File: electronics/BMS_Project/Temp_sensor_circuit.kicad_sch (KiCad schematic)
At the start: 0 parts

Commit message: added thermistor voltage divider to "temp_sensor_circuit"
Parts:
- added R29, R30, R31, R32: 100k, symbol Device:R
- added Temp_1, Temp_2, Temp_3, Temp_4: Prototyping_Pad_Data, BMS_lib:Prototyping_Pad_Data, symbol BMS_lib:Prototyping_Pad_Data
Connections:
- new net +5V: R29.2, R30.2, R31.2, R32.2
- new net Temp_1: R29.1, Temp_1.1
- new net Temp_2: R30.1, Temp_2.1
- new net Temp_3: R31.1, Temp_3.1
- new net Temp_4: R32.1, Temp_4.1

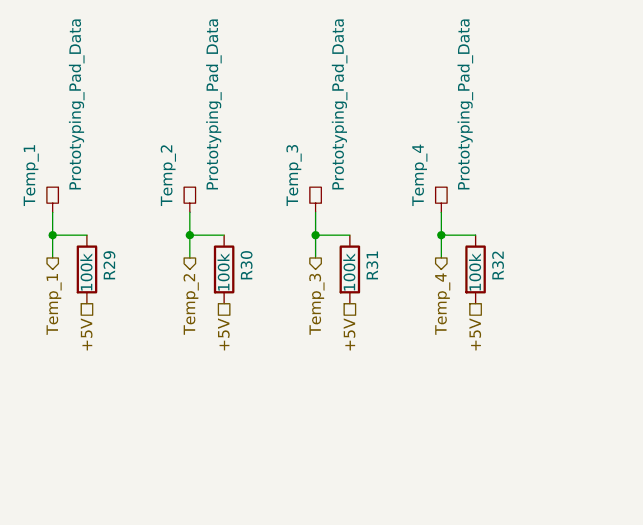
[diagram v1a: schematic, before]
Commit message: small tweaks to the labels
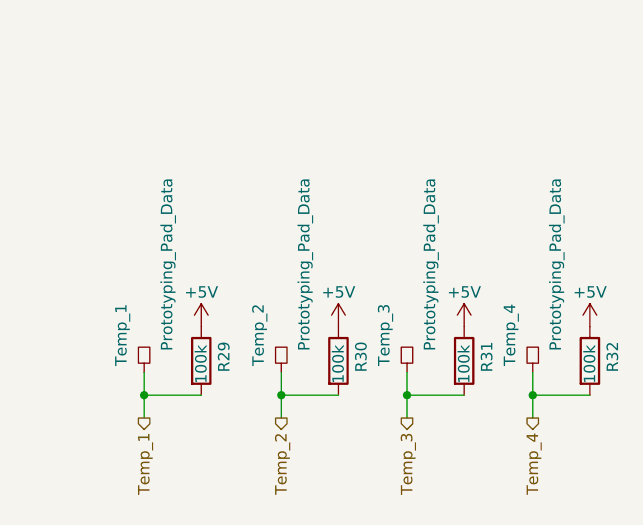
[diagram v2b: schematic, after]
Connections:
- net +5V: now also R29.1, R30.1, R31.1, R32.1; no longer R29.2, R30.2, R31.2, R32.2
- net Temp_1: now also R29.2; no longer R29.1
- net Temp_2: now also R30.2; no longer R30.1
- net Temp_3: now also R31.2; no longer R31.1
- net Temp_4: now also R32.2; no longer R32.1
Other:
- moved on the sheet: R29, R30, R31, R32, Temp_1, Temp_2, Temp_3, Temp_4

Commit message: Meeting 28.04.2023 worked on schematic
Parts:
- removed Temp_1, Temp_2, Temp_3, Temp_4: Prototyping_Pad_Data, BMS_lib:Prototyping_Pad_Data, symbol BMS_lib:Prototyping_Pad_Data
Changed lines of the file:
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@@
     (effects (font (size 1.27 1.27)) (justify right))
+  )
+  (hierarchical_label "sensor_3" (shape input) (at 80.01 50.8 90) (fields_autoplaced)
+    (effects (font (size 1.27 1.27)) (justify left))
+  )
+  (hierarchical_label "sensor_1" (shape input) (at 50.8 50.8 90) (fields_autoplaced)
+    (effects (font (size 1.27 1.27)) (justify left))
   )
   (hierarchical_label "Temp_3" (shape output) (at 80.01 55.88 270) (fields_autoplaced)
     (effects (font (size 1.27 1.27)) (justify right))
   )
+  (hierarchical_label "sensor_2" (shape input) (at 66.04 50.8 90) (fields_autoplaced)
+    (effects (font (size 1.27 1.27)) (justify left))
+  )
   (hierarchical_label "Temp_1" (shape output) (at 50.8 55.88 270) (fields_autoplaced)
     (effects (font (size 1.27 1.27)) (justify right))
   )
+  (hierarchical_label "sensor_4" (shape input) (at 93.98 50.8 90) (fields_autoplaced)
+    (effects (font (size 1.27 1.27)) (justify left))
+  )
   (hierarchical_label "Temp_2" (shape output) (at 66.04 55.88 270) (fields_autoplaced)
     (effects (font (size 1.27 1.27)) (justify right))
@@
     )
   )
-  (symbol (lib_id "BMS_lib:Prototyping_Pad_Data") (at 80.01 50.8 90) (unit 1)
-    (in_bom yes) (on_board yes) (dnp no)
-    (property "Reference" "Temp_3" (at 77.47 43.18 0)
-      (effects (font (size 1.27 1.27)) (justify right))
-    )
-    (property "Value" "Prototyping_Pad_Data" (at 82.55 29.21 0)
-      (effects (font (size 1.27 1.27)) (justify right))
-    )
-    (property "Footprint" "BMS_lib:Prototyping_Pad_Data" (at 76.2 46.99 0)
-      (effects (font (size 1.27 1.27)) hide)
-    )
-    (property "Datasheet" "" (at 80.01 50.8 0)
-      (effects (font (size 1.27 1.27)) hide)
-    )
-    (pin "1")
-    (instances
-      (project "BMS_Project"
-        (path "/524e7f14-feb0-4ca2-9425-a347c869bfa6/3ef60c79-05b1-4258-868e-74de6ac64829"
-          (reference "Temp_3") (unit 1)
-        )
-      )
-    )
-  )
-  (symbol (lib_id "BMS_lib:Prototyping_Pad_Data") (at 66.04 50.8 90) (unit 1)
-    (in_bom yes) (on_board yes) (dnp no)
-    (property "Reference" "Temp_2" (at 63.5 43.18 0)
-      (effects (font (size 1.27 1.27)) (justify right))
-    )
-    (property "Value" "Prototyping_Pad_Data" (at 68.58 29.21 0)
-      (effects (font (size 1.27 1.27)) (justify right))
-    )
-    (property "Footprint" "BMS_lib:Prototyping_Pad_Data" (at 62.23 46.99 0)
-      (effects (font (size 1.27 1.27)) hide)
-    )
-    (property "Datasheet" "" (at 66.04 50.8 0)
-      (effects (font (size 1.27 1.27)) hide)
-    )
-    (pin "1")
-    (instances
-      (project "BMS_Project"
-        (path "/524e7f14-feb0-4ca2-9425-a347c869bfa6/3ef60c79-05b1-4258-868e-74de6ac64829"
-          (reference "Temp_2") (unit 1)
-        )
-      )
-    )
-  )
-  (symbol (lib_id "BMS_lib:Prototyping_Pad_Data") (at 93.98 50.8 90) (unit 1)
-    (in_bom yes) (on_board yes) (dnp no)
-    (property "Reference" "Temp_4" (at 91.44 43.18 0)
-      (effects (font (size 1.27 1.27)) (justify right))
-    )
-    (property "Value" "Prototyping_Pad_Data" (at 96.52 29.21 0)
-      (effects (font (size 1.27 1.27)) (justify right))
-    )
-    (property "Footprint" "BMS_lib:Prototyping_Pad_Data" (at 90.17 46.99 0)
-      (effects (font (size 1.27 1.27)) hide)
-    )
-    (property "Datasheet" "" (at 93.98 50.8 0)
-      (effects (font (size 1.27 1.27)) hide)
-    )
-    (pin "1")
-    (instances
-      (project "BMS_Project"
-        (path "/524e7f14-feb0-4ca2-9425-a347c869bfa6/3ef60c79-05b1-4258-868e-74de6ac64829"
-          (reference "Temp_4") (unit 1)
-        )
-      )
-    )
-  )
   (symbol (lib_id "Device:R") (at 100.33 49.53 0) (unit 1)
     (in_bom yes) (on_board yes) (dnp no)
@@
         )
       )
-    )
-  )
-  (symbol (lib_id "BMS_lib:Prototyping_Pad_Data") (at 50.8 50.8 90) (unit 1)
-    (in_bom yes) (on_board yes) (dnp no)
-    (property "Reference" "Temp_1" (at 48.26 43.18 0)
-      (effects (font (size 1.27 1.27)) (justify right))
-    )
-    (property "Value" "Prototyping_Pad_Data" (at 53.34 29.21 0)
-      (effects (font (size 1.27 1.27)) (justify right))
-    )
-    (property "Footprint" "BMS_lib:Prototyping_Pad_Data" (at 46.99 46.99 0)
-      (effects (font (size 1.27 1.27)) hide)
-    )
-    (property "Datasheet" "" (at 50.8 50.8 0)
-      (effects (font (size 1.27 1.27)) hide)
-    )
-    (pin "1")
-    (instances
-      (project "BMS_Project"
-        (path "/524e7f14-feb0-4ca2-9425-a347c869bfa6/3ef60c79-05b1-4258-868e-74de6ac64829"
-          (reference "Temp_1") (unit 1)
-        )
-      )

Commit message: discord session with Johannes and Fabian, Schematic nearly done, all footprints fields filled
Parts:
- R29, R30, R31, R32: footprint (none) -> Resistor_SMD:R_0805_2012Metric
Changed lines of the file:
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@@
       (effects (font (size 1.27 1.27)) (justify left))
     )
-    (property "Footprint" "" (at 55.372 49.53 90)
+    (property "Footprint" "Resistor_SMD:R_0805_2012Metric" (at 55.372 49.53 90)
       (effects (font (size 1.27 1.27)) hide)
     )
@@
       (effects (font (size 1.27 1.27)) (justify left))
     )
-    (property "Footprint" "" (at 98.552 49.53 90)
+    (property "Footprint" "Resistor_SMD:R_0805_2012Metric" (at 98.552 49.53 90)
       (effects (font (size 1.27 1.27)) hide)
     )
@@
       (effects (font (size 1.27 1.27)) (justify left))
     )
-    (property "Footprint" "" (at 70.612 49.53 90)
+    (property "Footprint" "Resistor_SMD:R_0805_2012Metric" (at 70.612 49.53 90)
       (effects (font (size 1.27 1.27)) hide)
     )
@@
       (effects (font (size 1.27 1.27)) (justify left))
     )
-    (property "Footprint" "" (at 84.582 49.53 90)
+    (property "Footprint" "Resistor_SMD:R_0805_2012Metric" (at 84.582 49.53 90)
       (effects (font (size 1.27 1.27)) hide)
     )
